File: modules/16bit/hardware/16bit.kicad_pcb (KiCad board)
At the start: 4 copper layers, 29 x 110 mm, 99 parts, among them J1 PJ301M-12, J2 PJ301M-12, J3 PJ301M-12, J4 PJ301M-12, J5 PJ301M-12, J6 Eurorack_2x5, J7 USB-C, Q1 MMBT3904, SW1 MODE, SW2 BOOT, SW3 RUN, U1 RP2350A, U2 W25Q128JVS, U3 APS6404L-3SQR-SN, U4 PT8211, U5 TL074, U6 MCP6002, U7 TL072, U8 AMS1117-5.0, U9 AMS1117-3.3, Y1 12MHz

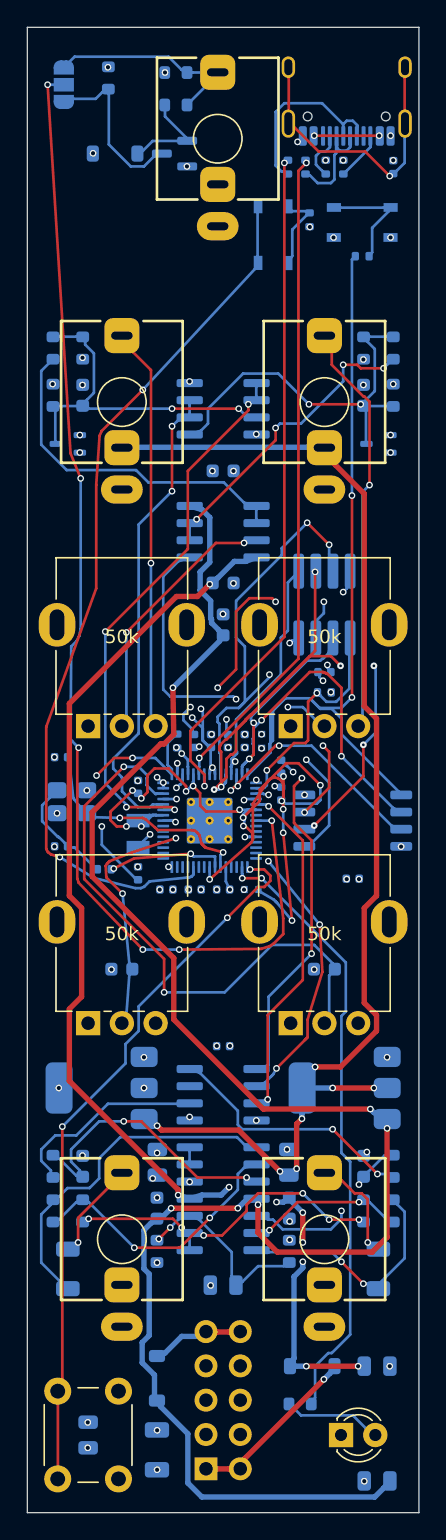
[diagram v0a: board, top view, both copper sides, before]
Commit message: 16bit: review pass — 9 in-pad vias moved off pads, jog cleanup, POFV fab requirement
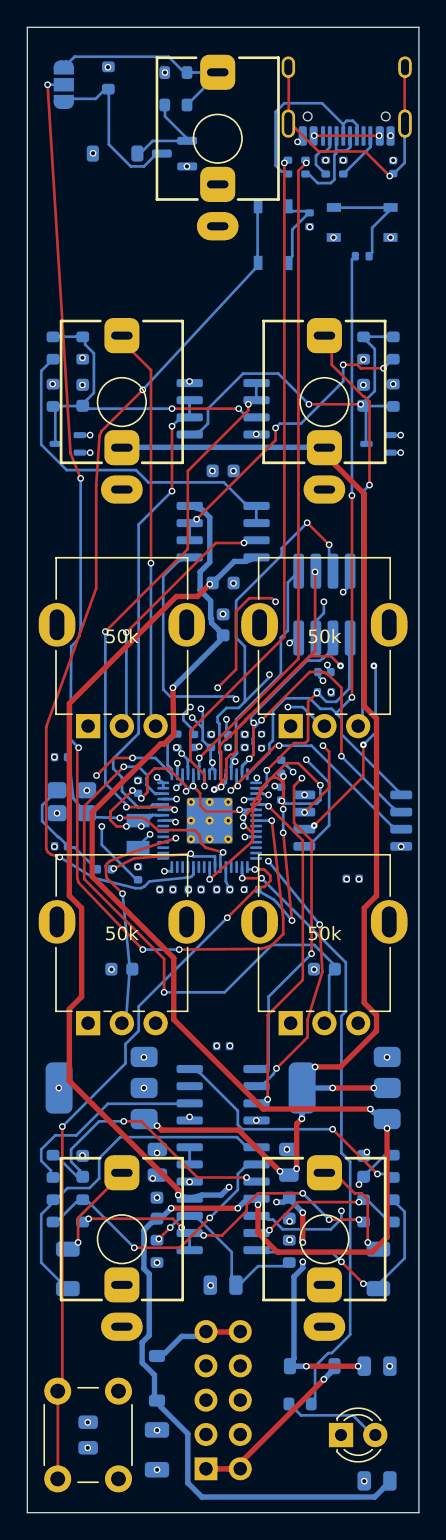
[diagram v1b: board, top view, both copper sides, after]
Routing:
- net /QSPI_SS: track 62.4 -> 53.5 mm
- net GND: track 9.05 -> 10.6 mm
- net +1V1: track 69.8 -> 68.7 mm
- net +3V3: track 18.6 -> 19.6 mm, vias 39 -> 38
- net Net-(J7-D--PadA7): track 8.67 -> 7.76 mm
- net /QSPI_SD3: track 43.2 -> 42.6 mm
- net /PSRAM_CS: track 17.2 -> 16.6 mm
